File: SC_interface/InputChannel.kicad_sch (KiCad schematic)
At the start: 42 parts, among them J201 Input, J202 BalancedOut, J203 Output_BNC, SW201 SW_Select1, U201 DRV135UA, U202 U2 OPA1656IDR, U203 INA134UA

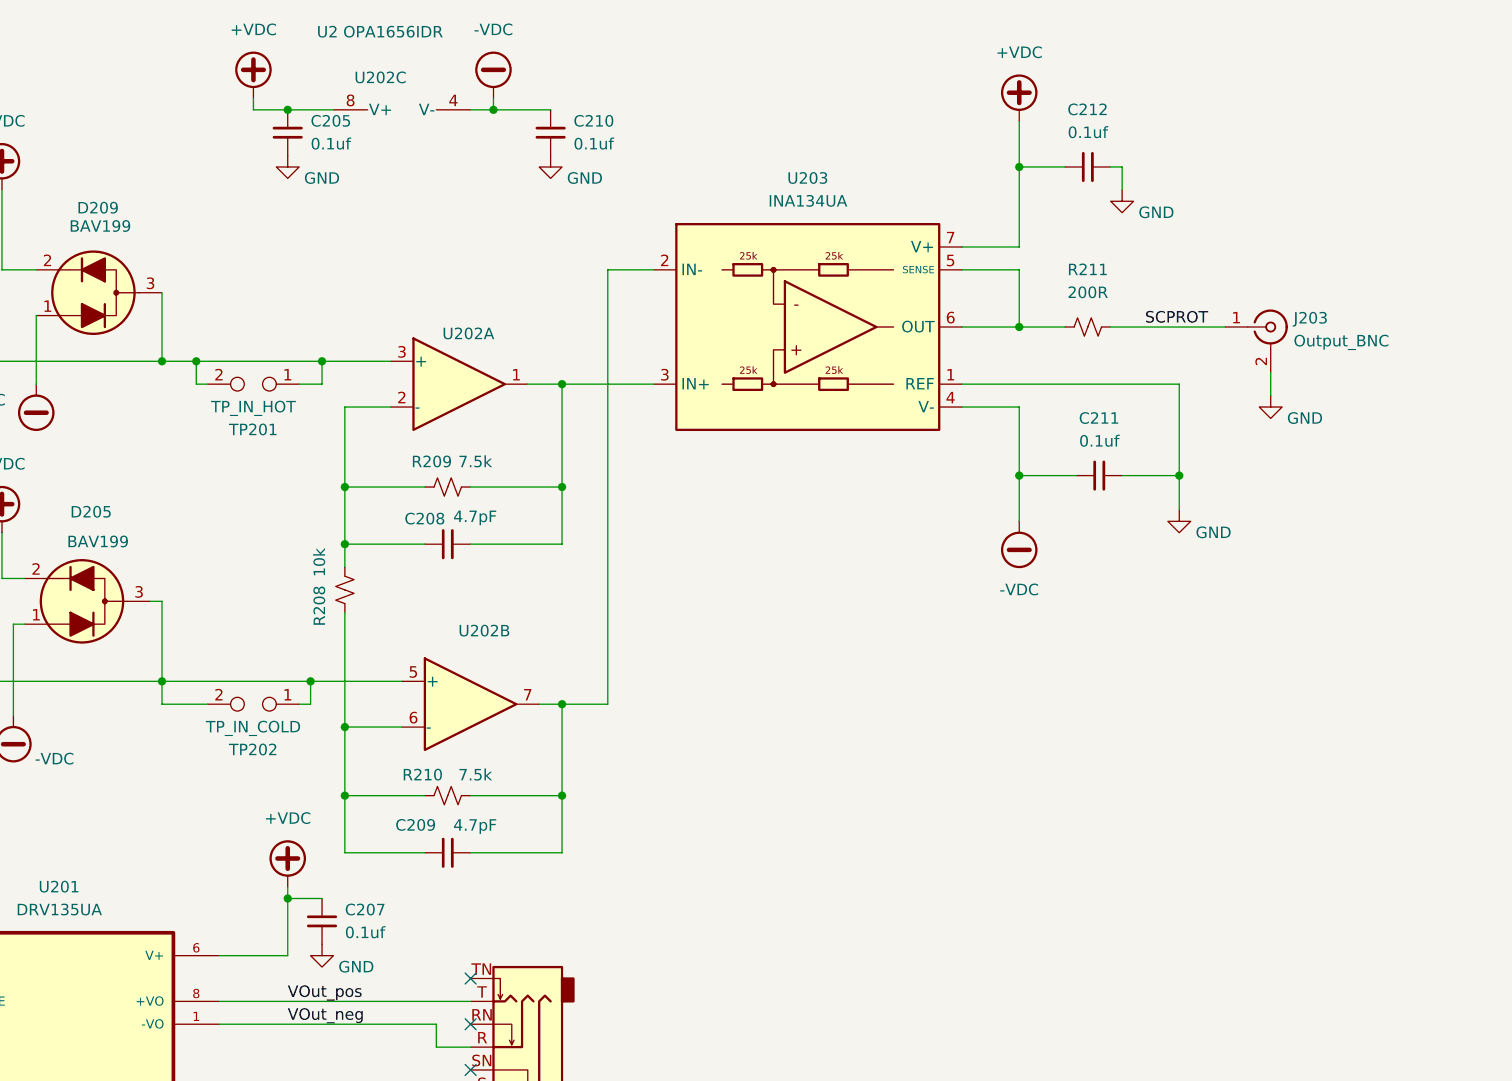
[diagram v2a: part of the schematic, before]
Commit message: design doc updated
1. 2.5mHz update.
C feedback. input stage change, clamping diodes,
rotary switch and R ladder, wire selection
Removed LND in favor of using 4.7 K fuseable R
Power supply switch, kick back TVS,
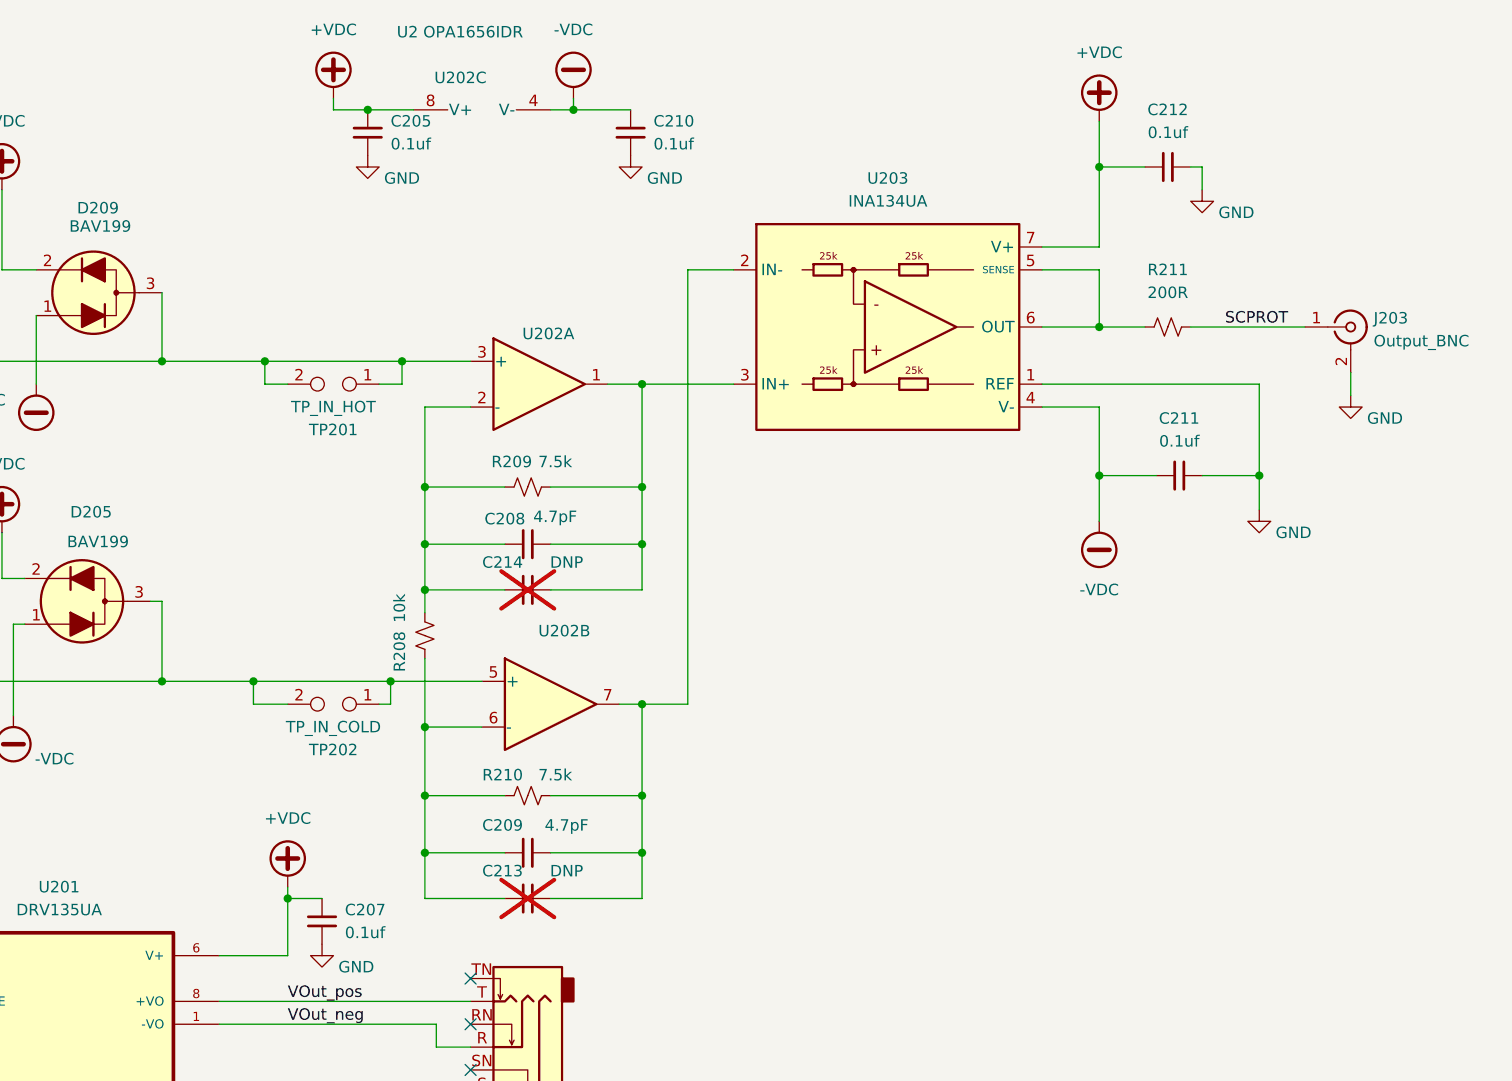
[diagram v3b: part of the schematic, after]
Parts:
- added C213, C214: DNP, Capacitor_SMD:C_0805_2012Metric_Pad1.18x1.45mm_HandSolder, symbol Device:C_Small
- R212, R213: footprint Resistor_THT:R_Axial_DIN0207_L6.3mm_D2.5mm_P15.24mm_Horizontal -> Project_Parts:R_Axial_DIN0207_P15.24mm_Socketed_NFR25; PROD_ID RES-07856 -> Vishay NFR25
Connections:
- net at C209.1, R208.1, R210.1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: now also C213.1
- net at C209.2, R210.2, U202.7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: now also C213.2
- net at C208.2, R209.2, U202.1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: now also C214.2
- net at C208.1, R208.2, R209.1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: now also C214.1
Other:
- moved on the sheet: C205, C208, C209, C210, C211, C212, J203, R208, R209, R210, R211, TP201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

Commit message: change the R ladder and switch to pin head
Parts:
- added J204: Frt_SW, Connector_JST:JST_XH_S5B-XH-A-1_1x05_P2.50mm_Horizontal, symbol Connector:Conn_01x05_Pin
- C202, C203: footprint Capacitor_THT:C_Rect_L13.0mm_W4.0mm_P10.00mm_FKS3_FKP3_MKS4 -> Capacitor_THT:C_Rect_L18.0mm_W7.0mm_P15.00mm_FKS3_FKP3
- J201: footprint Connector_PinHeader_2.54mm:PinHeader_1x02_P2.54mm_Vertical -> Connector_JST:JST_XH_S3B-XH-A-1_1x03_P2.50mm_Horizontal
- R202: footprint Resistor_SMD:R_MELF_MMB-0207 -> Resistor_THT:R_Axial_DIN0207_L6.3mm_D2.3mm_P7.62mm_Horizontal; MPN (none) -> CMF5590K900FHEB; Manufacturer (none) -> Vishay Dale; PROD_ID RES-07856 -> CMF90.9KHFCT-ND
- R203: footprint Resistor_SMD:R_1206_3216Metric_Pad1.30x1.75mm_HandSolder -> Resistor_THT:R_Axial_DIN0207_L6.3mm_D2.3mm_P7.62mm_Horizontal; MPN (none) -> CMF559K0900FHEB; Manufacturer (none) -> Vishay Dale
- R204: footprint Resistor_SMD:R_0805_2012Metric_Pad1.20x1.40mm_HandSolder -> Resistor_THT:R_Axial_DIN0207_L6.3mm_D2.3mm_P7.62mm_Horizontal; MPN (none) -> CMF55909R00FHEB; Manufacturer (none) -> Vishay Dale
- SW201: value SW_Select1 -> Select SW; footprint Connector_PinHeader_2.54mm:PinHeader_1x05_P2.54mm_Vertical -> Panel_Mount:RotarySwitch_1P4T_PanelMount; MPN (none) -> KC14A13.001NLS; Manufacturer (none) -> E-Switch
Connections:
- net GND: now also J204.2 (Pin_2), J204.4 (Pin_4)
- net at R202.2, SW201.1: no longer C202.2
- net at R204.1, SW201.4: no longer R205.2
- net at SW201.5: no longer R212.1
- new net Input_cold: J204.3 (Pin_3), R205.2
- new net Input_hot: C202.2, J204.1 (Pin_1)
- new net Input_wiper: J204.5 (Pin_5), R212.1
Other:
- moved on the sheet: R202, R203, R204, SW201
